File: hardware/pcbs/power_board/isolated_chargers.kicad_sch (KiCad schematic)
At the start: 4 parts

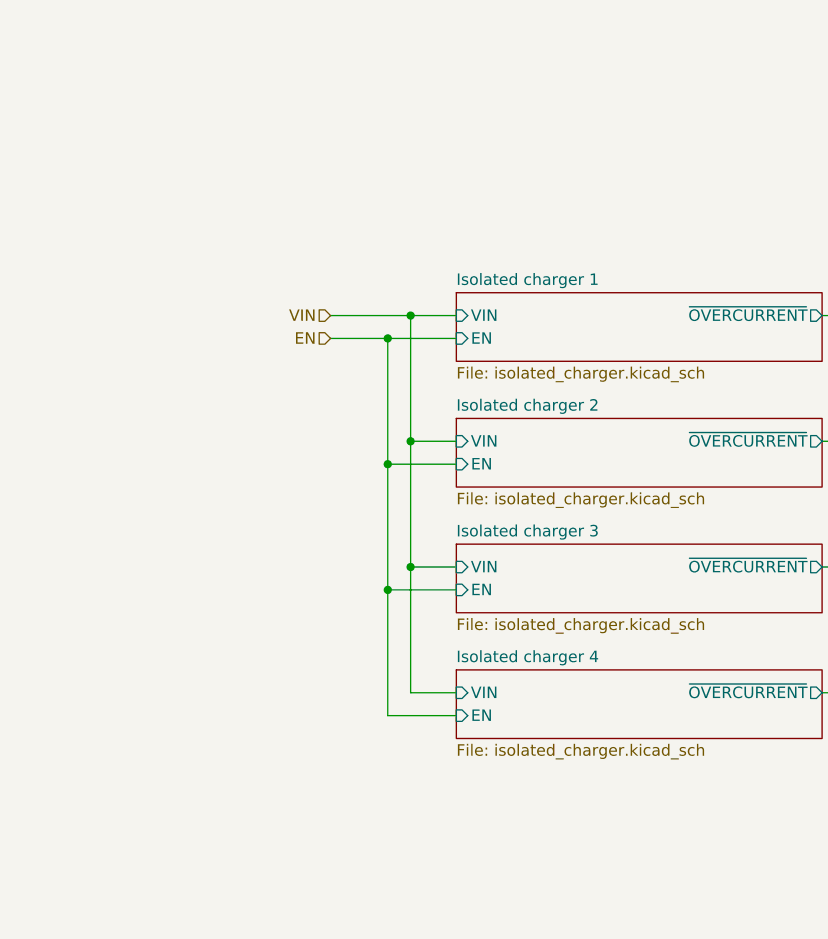
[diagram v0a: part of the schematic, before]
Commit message: power_board: add temperature sensor and GPIOs to schematic
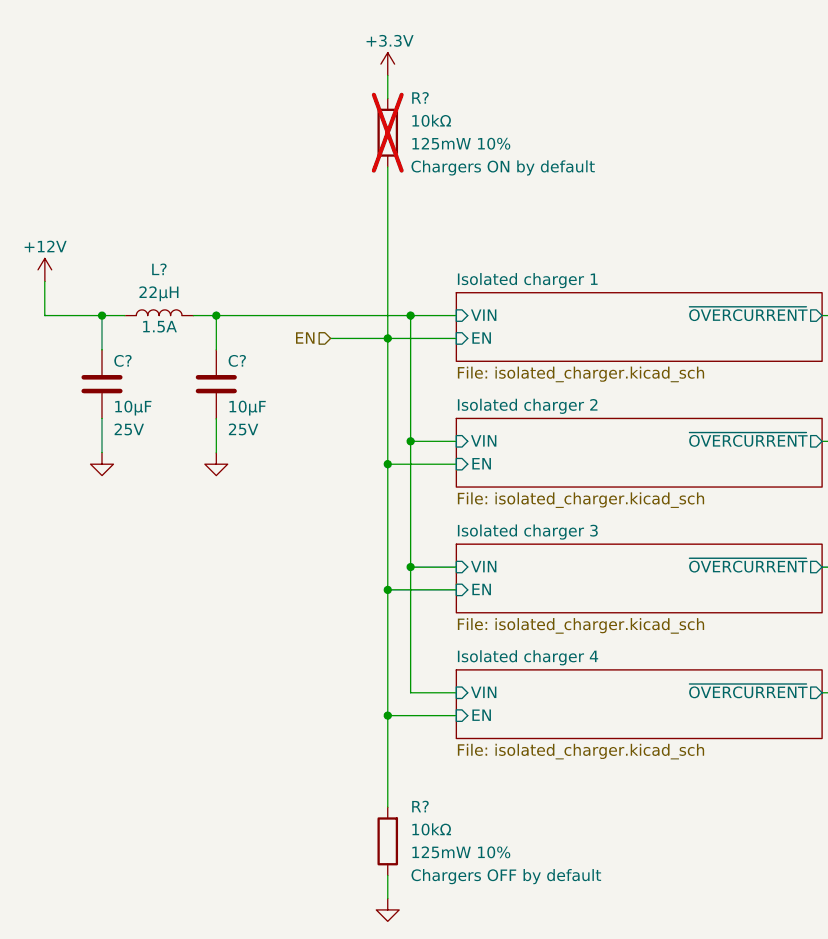
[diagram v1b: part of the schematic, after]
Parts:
- added C? (x2): 10μF, Capacitor_SMD:C_0805_2012Metric, symbol Device:C
- added L?: 22μH, Inductor_SMD:L_Sunlord_SWPA6045S, symbol Device:L
- added R? (x2): 10kΩ, Resistor_SMD:R_0805_2012Metric, symbol Device:R
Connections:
- net +3.3V: now also R?.2
- net EN: now also R?.1, R?.2
- net GND: now also C?.2, C?.2, R?.1
- new net +12V: C?.1, L?.1
- new net Isolated charger 1/VIN: C?.1, L?.2

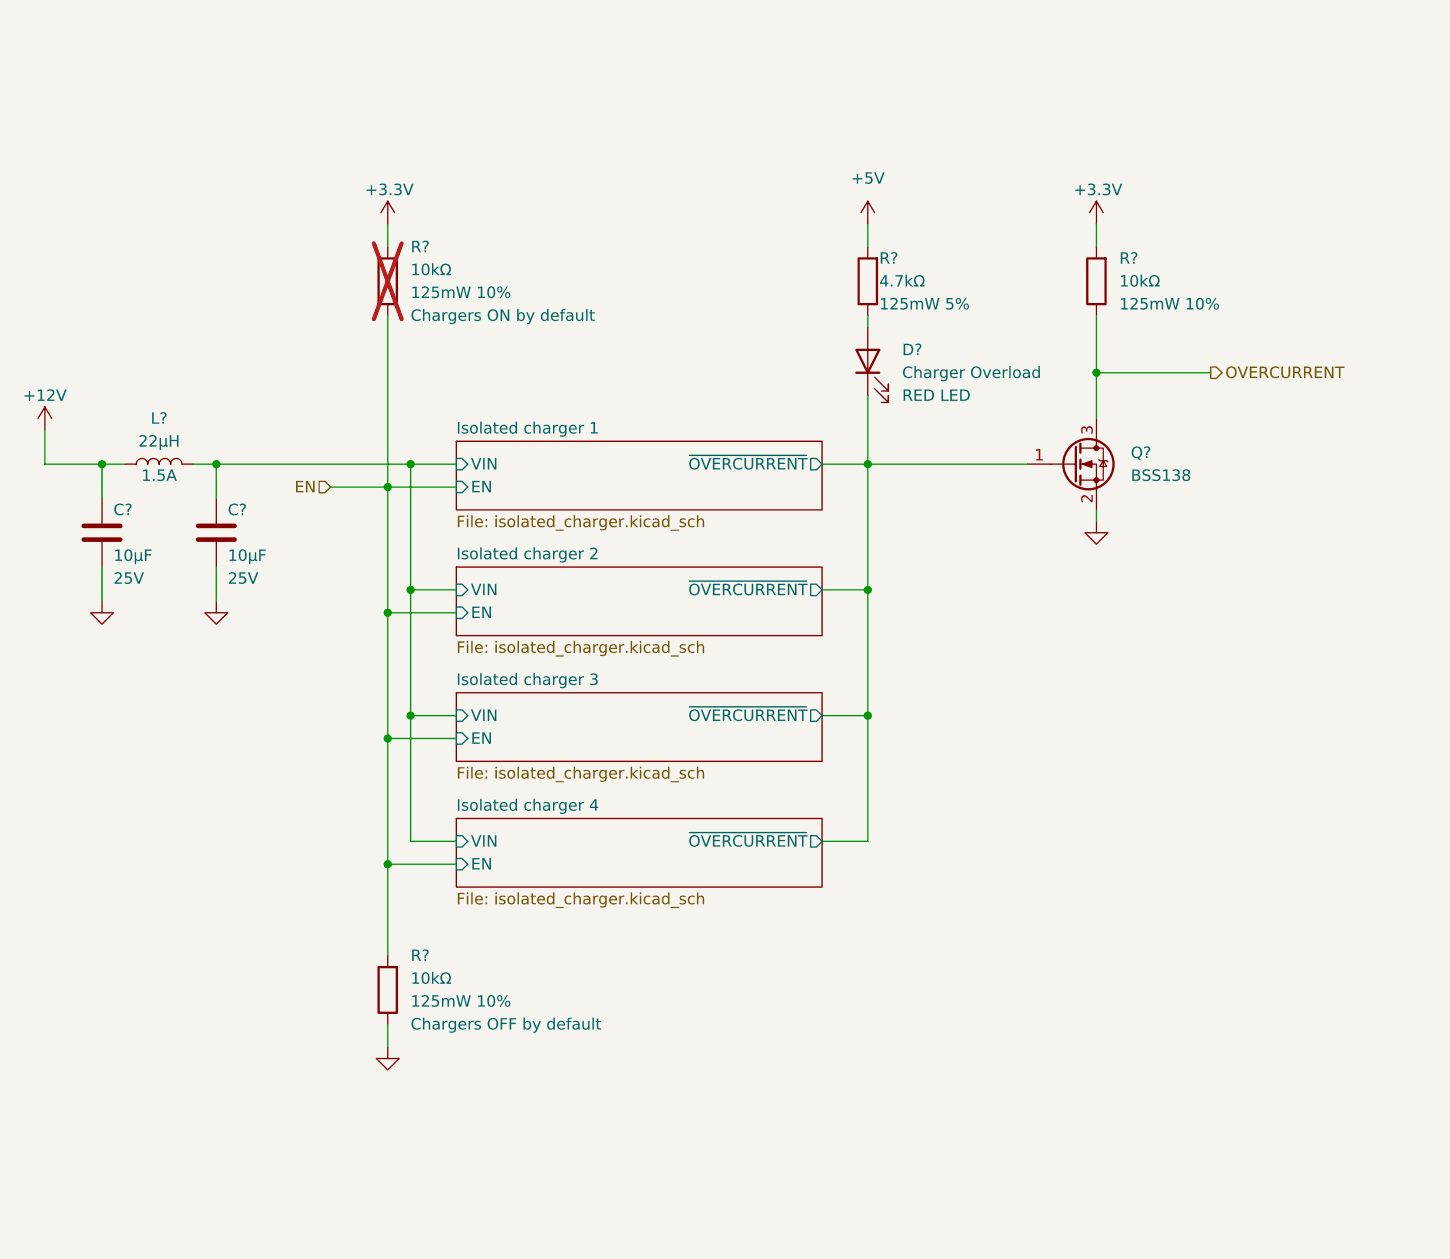
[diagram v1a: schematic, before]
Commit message: power_board: minor fixes to shematic
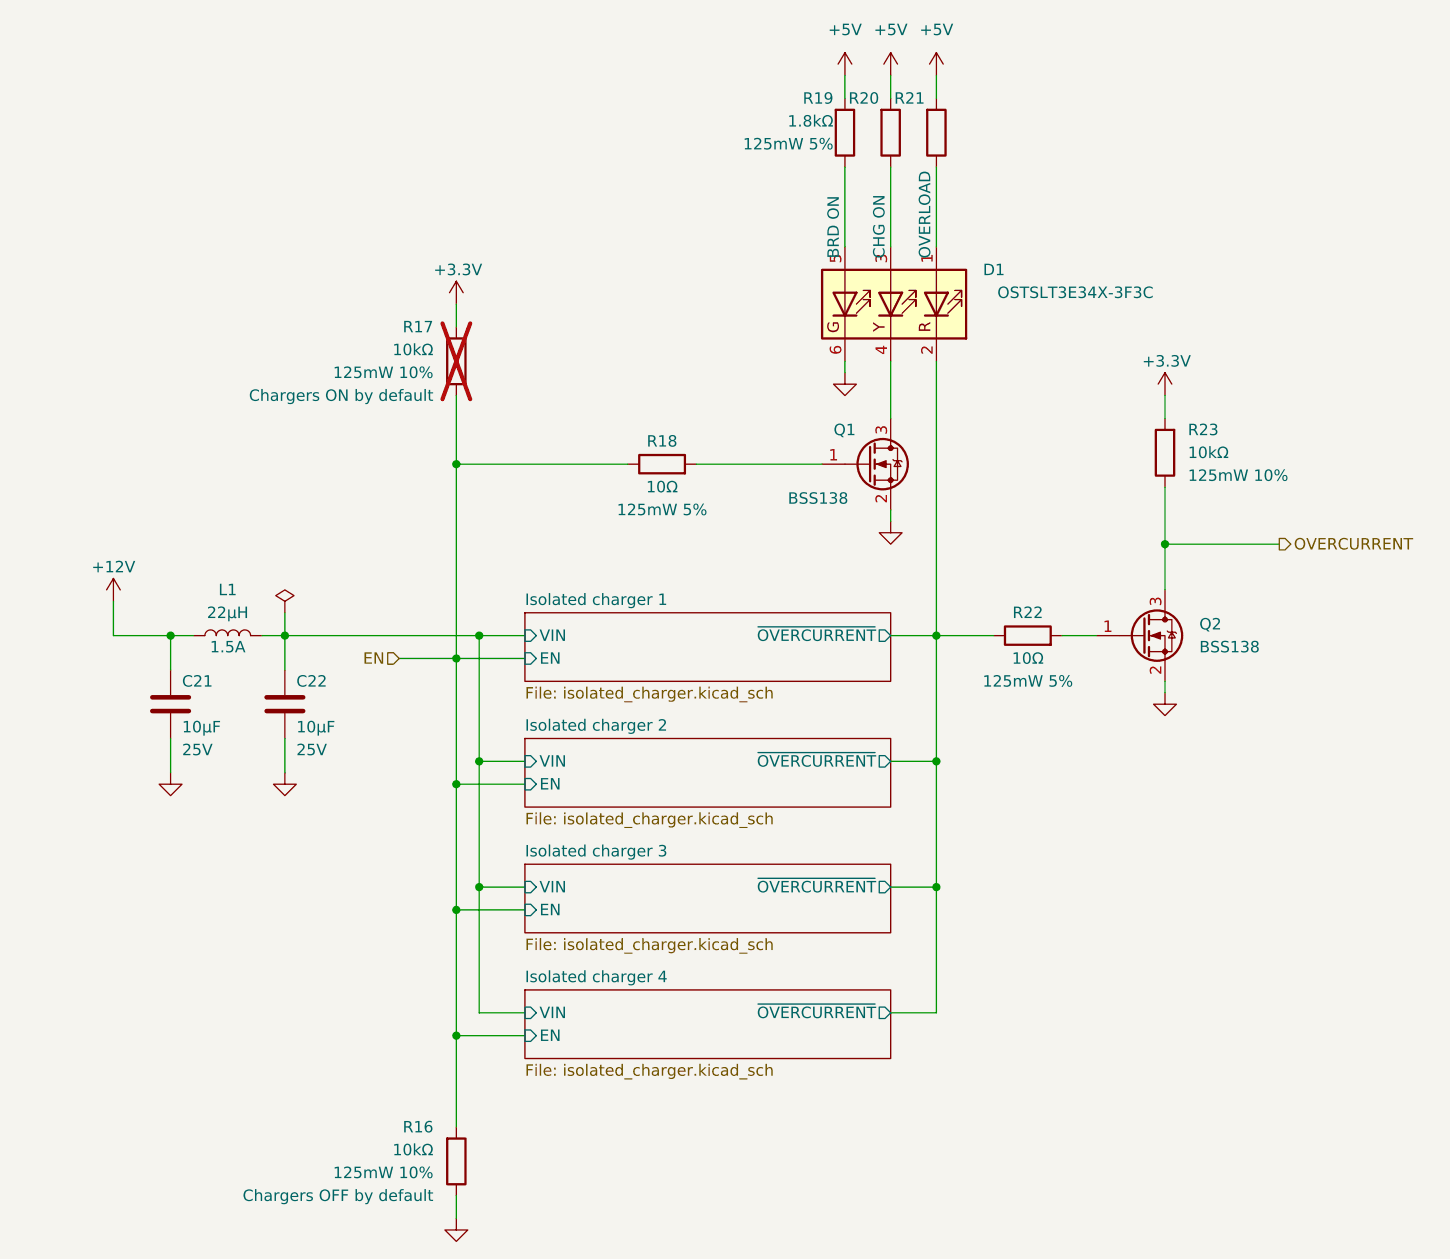
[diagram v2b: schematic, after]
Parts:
- removed D?: RED LED, LED_THT:LED_D3.0mm, symbol Device:LED
- removed R?: 4.7kΩ, Resistor_SMD:R_0805_2012Metric, symbol Device:R
- added D1: OSTSLT3E34X-3F3C, extra:OSTSLT3E34X-3F3C, symbol extra:LED_RYG
- added Q1: BSS138, Package_TO_SOT_SMD:SOT-23, symbol Transistor_FET:BSS138
- added R18, R22: 10Ω, Resistor_SMD:R_0805_2012Metric, symbol Device:R
- added R19, R20, R21: 1.8kΩ, Resistor_SMD:R_0805_2012Metric, symbol Device:R
- gave numbers to parts that had none: 7
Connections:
- net +5V: now also R19.2, R20.2, R21.2
- net EN: now also R18.1
- net GND: now also D1.6 (GK), Q1.2 (S)
- net Isolated charger 1/~{OVERCURRENT}: now also D1.2 (RK), R22.1; no longer Q2.1 (G)
- new net: Q2.1 (G), R22.2
- new net: D1.1 (RA), R21.1
- new net: D1.3 (YA), R20.1
- new net: D1.4 (YK), Q1.3 (D)
- new net: D1.5 (GA), R19.1
- new net: Q1.1 (G), R18.2
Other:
- moved on the sheet: C21, C22, L1, Q2, R16, R17, R23

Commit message: power_board: connect power led to SBC's usb and fix inductor values
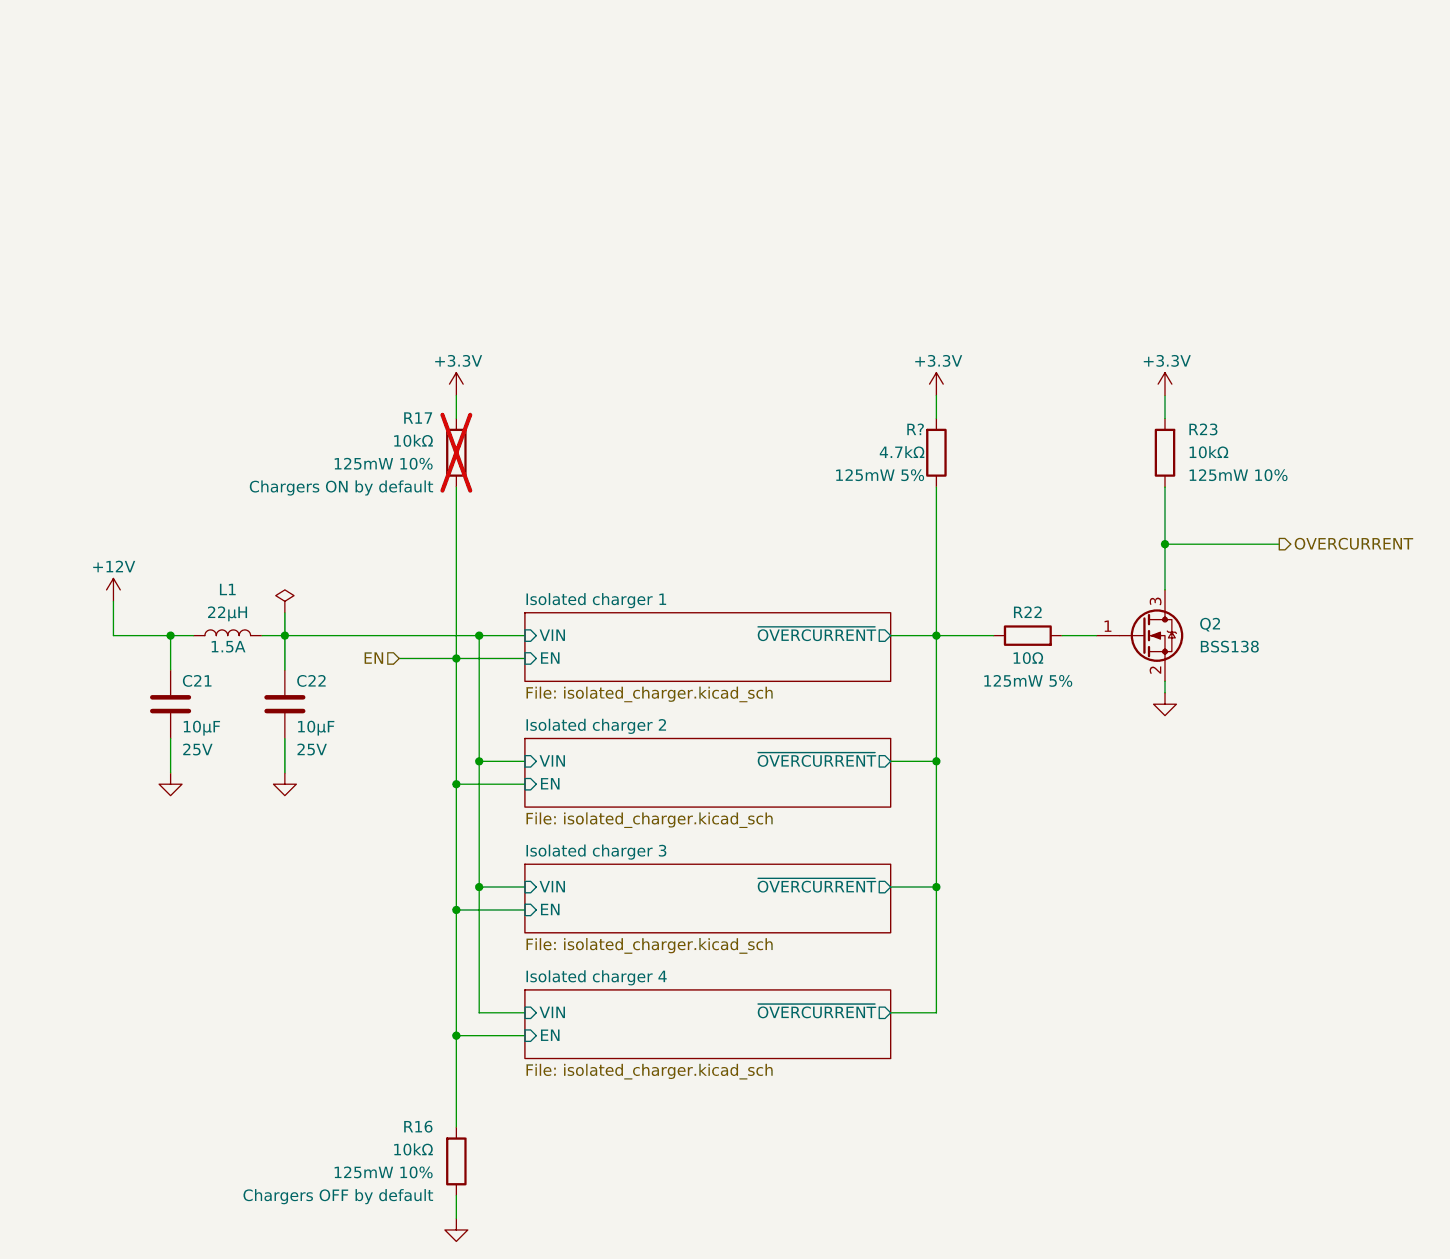
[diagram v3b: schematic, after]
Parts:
- removed D1: OSTSLT3E34X-3F3C, extra:OSTSLT3E34X-3F3C, symbol extra:LED_RYG
- removed Q1: BSS138, Package_TO_SOT_SMD:SOT-23, symbol Transistor_FET:BSS138
- removed R18: 10Ω, Resistor_SMD:R_0805_2012Metric, symbol Device:R
- removed R19, R20, R21: 1.8kΩ, Resistor_SMD:R_0805_2012Metric, symbol Device:R
- added R?: 4.7kΩ, Resistor_SMD:R_0805_2012Metric, symbol Device:R
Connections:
- net +3.3V: now also R?.2
- net Isolated charger 1/~{OVERCURRENT}: now also R?.1
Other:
- moved on the sheet: R17

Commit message: power_board: finalise all footprints
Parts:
- gave numbers to parts that had none: 1
- renumbered C21 to C22, C22 to C23, Q2 to Q1, R17 to R16, R16 to R17, R22 to R19, R23 to R20

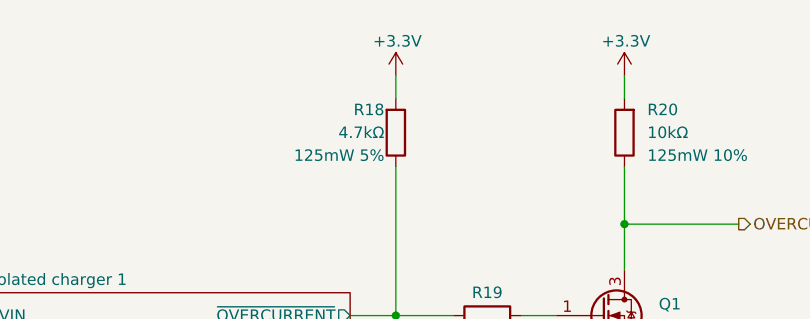
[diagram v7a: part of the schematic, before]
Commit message: power_board: remove unused caps
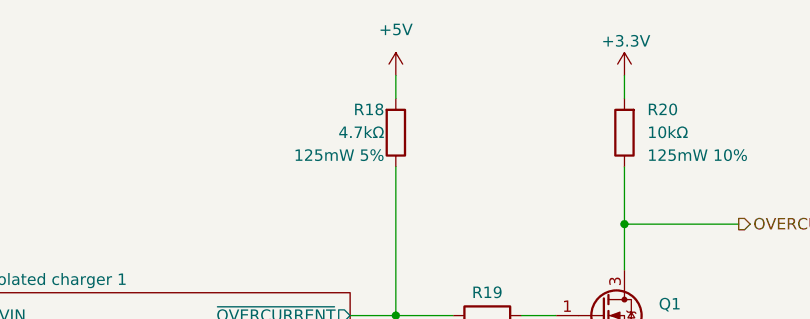
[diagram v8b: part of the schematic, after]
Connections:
- net +3.3V: no longer R18.2
- new net +5V: R18.2
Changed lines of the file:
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@@
+	)
+	(symbol
+		(lib_id "power:+5V")
+		(at 160.02 74.93 0)
+		(unit 1)
+		(exclude_from_sim no)
+		(in_bom yes)
+		(on_board yes)
+		(dnp no)
+		(fields_autoplaced yes)
+		(property "Reference" "#PWR028"
+			(at 160.02 78.74 0)
+			(effects
+				(font
+					(size 1.27 1.27)
+				)
+				(hide yes)
+			)
+		)
+		(property "Value" "+5V"
+			(at 160.02 69.85 0)
+			(effects
+				(font
+					(size 1.27 1.27)
+				)
+			)
+		)
+		(property "Footprint" ""
+			(at 160.02 74.93 0)
+			(effects
+				(font
+					(size 1.27 1.27)
+				)
+				(hide yes)
+			)
+		)
+		(property "Datasheet" ""
+			(at 160.02 74.93 0)
+			(effects
+				(font
+					(size 1.27 1.27)
+				)
+				(hide yes)
+			)
+		)
+		(property "Description" ""
+			(at 160.02 74.93 0)
+			(effects
+				(font
+					(size 1.27 1.27)
+				)
+				(hide yes)
+			)
+		)
+		(pin "1"
+		)
+		(instances
+			(project "power_board"
+				(path "/4b166175-80a4-48c6-994d-6e62a6160b87/2e2b9578-5dbd-4b2d-88fb-256ac9c8dd75"
+					(reference "#PWR028")
+					(unit 1)
+				)
+			)
+		)
 	)
 	(symbol
@@
 					(unit 1)
 				)
-			)
-		)
-	)
-	(symbol
-		(lib_id "power:+3.3V")
-		(at 160.02 74.93 0)
-		(unit 1)
-		(exclude_from_sim no)
-		(in_bom yes)
-		(on_board yes)
-		(dnp no)
-		(property "Reference" "#PWR028"
-			(at 160.02 78.74 0)
-			(effects
-				(font
-					(size 1.27 1.27)
-				)
-				(hide yes)
-			)
-		)
-		(property "Value" "+3.3V"
-			(at 157.48 71.12 0)
-			(effects
-				(font
-					(size 1.27 1.27)
-				)
-				(justify left)
-			)
-		)
-		(property "Footprint" ""
-			(at 160.02 74.93 0)
-			(effects
-				(font
-					(size 1.27 1.27)
-				)
-				(hide yes)
-			)
-		)
-		(property "Datasheet" ""
-			(at 160.02 74.93 0)
-			(effects
-				(font
-					(size 1.27 1.27)
-				)
-				(hide yes)
-			)
-		)
-		(property "Description" ""
-			(at 160.02 74.93 0)
-			(effects
-				(font
-					(size 1.27 1.27)
-				)
-				(hide yes)
-			)
-		)
-		(pin "1"
-		)
-		(instances
-			(project "power_board"
-				(path "/4b166175-80a4-48c6-994d-6e62a6160b87/2e2b9578-5dbd-4b2d-88fb-256ac9c8dd75"
-					(reference "#PWR028")
-					(unit 1)
-				)
